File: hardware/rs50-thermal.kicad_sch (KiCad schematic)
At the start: 0 parts

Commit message: feat(hw): adiciona 22 componentes ao schematic RS50
- Power input: J1, F1, D1, U1 (LM2596S-5), L1, C1, C2
- Sensor NTC: R1, TH1, C3
- MCU: U2 (ESP32-S3-Zero), SW1, SW2, D2, R2
- Potencia: R3, R4, Q1 (NMOS), K1 (rele SPDT), D3, J2
- Corrige sym-lib-table apontando para /symbols/

Sub-etapa 4.2 concluida
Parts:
- added C1, C2: C_Polarized, symbol Device:C_Polarized
- added C3: C, symbol Device:C
- added D1: D_Schottky, symbol Device:D_Schottky
- added D2: LED, symbol Device:LED
- added D3: D, symbol Device:D
- added F1: Fuse, symbol Device:Fuse
- added J1, J2: Conn_01x02, symbol Connector_Generic:Conn_01x02
- added K1: Relay_SPDT, symbol Relay:Relay_SPDT
- added L1: L, symbol Device:L
- added Q1: Q_NMOS_GDS, symbol Transistor_FET:Q_NMOS_GDS
- added R1, R2, R3, R4: R, symbol Device:R
- added SW1, SW2: SW_Push, symbol Switch:SW_Push
- added TH1: Thermistor_NTC, symbol Device:Thermistor_NTC
- added U1: LM2596S-5, Package_TO_SOT_SMD:TO-263-5_TabPin3, symbol Regulator_Switching:LM2596S-5
- added U2: ESP32-S3-Zero, rs50-custom:Module_ESP32-S3-Zero_2x11_Header, symbol rs50-custom:ESP32-S3-Zero
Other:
- company: (none) -> DrEaD
- title: (none) -> RS50 Thermal Controller

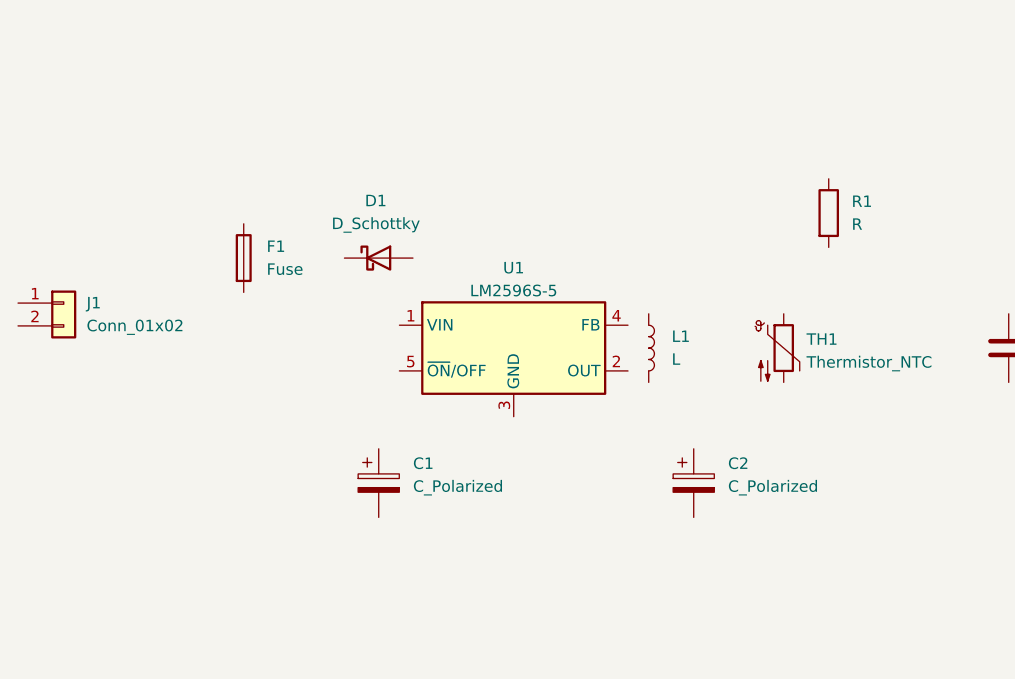
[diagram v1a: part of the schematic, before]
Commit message: feat(hw): refatora schematic para modulo HW-411 + XT60
- Substitui LM2596 discreto (U1+L1+C1+C2+D1) por modulo Buck HW-411
- Substitui J1 generico por conector XT60 (entrada 24V)
- Atualiza .gitignore (estava staged mas nao commitado)
- Mantem F1 Fuse na entrada para protecao
- Schematic agora usado como diagrama de montagem (nao PCB fab)

Reduz contagem de 22 para 18 componentes
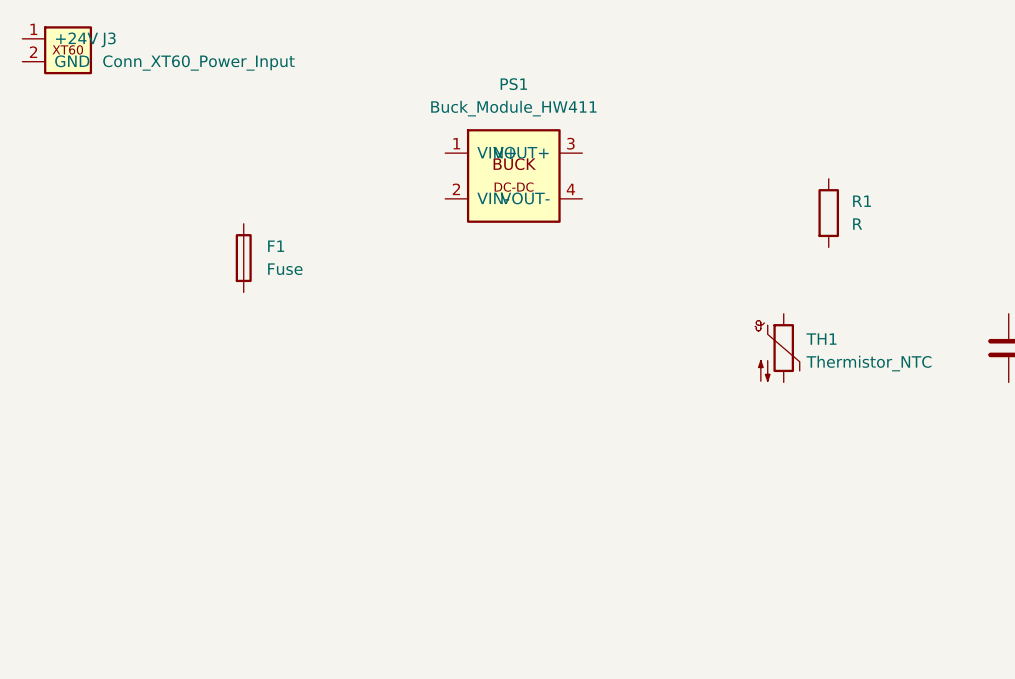
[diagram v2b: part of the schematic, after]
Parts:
- removed C1, C2: C_Polarized, symbol Device:C_Polarized
- removed D1: D_Schottky, symbol Device:D_Schottky
- removed J1: Conn_01x02, symbol Connector_Generic:Conn_01x02
- removed L1: L, symbol Device:L
- removed U1: LM2596S-5, Package_TO_SOT_SMD:TO-263-5_TabPin3, symbol Regulator_Switching:LM2596S-5
- added J3: Conn_XT60_Power_Input, rs50-custom:Conn_XT60_PCB_Mount, symbol rs50-custom:Conn_XT60_Power_Input
- added PS1: Buck_Module_HW411, rs50-custom:Buck_Module_HW411_4pin_P2.54mm, symbol rs50-custom:Buck_Module_HW411
